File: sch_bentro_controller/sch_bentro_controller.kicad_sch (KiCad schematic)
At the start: 11 parts, among them J1 Barrel_Jack, J2 Screw_Terminal_01x02, Q1 BSS214, SW1 SW_Push, SW2 RockerSwitch

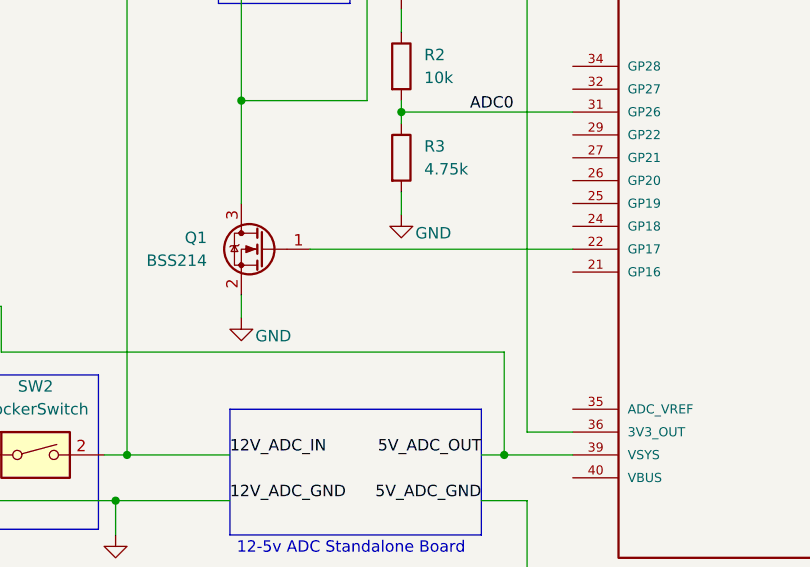
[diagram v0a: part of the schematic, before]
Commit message: added Gate pull down resistor
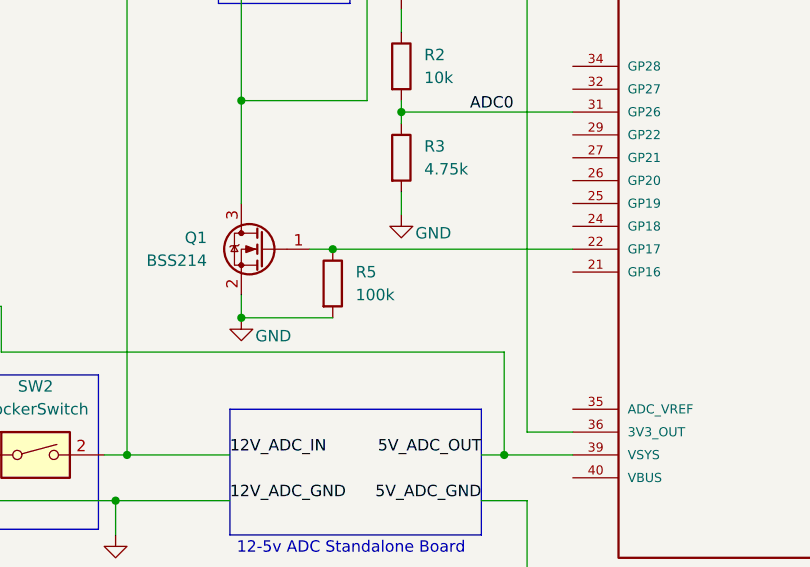
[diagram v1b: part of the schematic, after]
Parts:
- added R5: 100k, symbol Device:R
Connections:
- net GND: now also R5.2
- net at A1.22 (GP17), Q1.1 (G): now also R5.1
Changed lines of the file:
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@@
+	)
+	(junction
+		(at 106.68 111.76)
+		(diameter 0)
+		(color 0 0 0 0)
 	)
 	(junction
@@
 	)
 	(junction
+		(at 96.52 119.38)
+		(diameter 0)
+		(color 0 0 0 0)
+	)
+	(junction
 		(at 125.73 134.62)
 		(diameter 0)
@@
 	(wire
 		(pts
-			(xy 104.14 111.76) (xy 133.35 111.76)
+			(xy 104.14 111.76) (xy 106.68 111.76)
 		)
 		(stroke
@@
 	(wire
 		(pts
+			(xy 96.52 119.38) (xy 106.68 119.38)
+		)
+		(stroke
+			(width 0)
+			(type default)
+		)
+	)
+	(wire
+		(pts
 			(xy 195.58 154.94) (xy 195.58 153.67)
 		)
@@
 		(pts
 			(xy 184.15 91.44) (xy 199.39 91.44)
+		)
+		(stroke
+			(width 0)
+			(type default)
+		)
+	)
+	(wire
+		(pts
+			(xy 106.68 111.76) (xy 133.35 111.76)
 		)
 		(stroke
@@
 					(unit 1)
 				)
+			)
+		)
+	)
+	(symbol
+		(lib_id "Device:R")
+		(at 106.68 115.57 0)
+		(unit 1)
+		(exclude_from_sim no)
+		(in_bom yes)
+		(on_board yes)
+		(dnp no)
+		(fields_autoplaced yes)
+		(property "Reference" "R5"
+			(at 109.22 114.2999 0)
+			(effects
+				(font
+					(size 1.27 1.27)
+				)
+				(justify left)
+			)
+		)
+		(property "Value" "100k"
+			(at 109.22 116.8399 0)
+			(effects
+				(font
+					(size 1.27 1.27)
+				)
+				(justify left)
+			)
+		)
+		(property "Footprint" ""
+			(at 104.902 115.57 90)
+			(effects
+				(font
+					(size 1.27 1.27)
+				)
+				(hide yes)
+			)
+		)
+		(property "Datasheet" "~"
+			(at 106.68 115.57 0)
+			(effects
+				(font
+					(size 1.27 1.27)
+				)
+				(hide yes)
+			)
+		)
+		(property "Description" "Resistor"
+			(at 106.68 115.57 0)
+			(effects
+				(font
+					(size 1.27 1.27)
+				)
+				(hide yes)
+			)
+		)
+		(pin "2"
+		)
+		(pin "1"
+		)
+		(instances
+			(project "sch_bentro_controller"
+				(path "/4c494bf6-61ac-4c54-bb68-d6309caa82e3"
+					(reference "R5")
+					(unit 1)
+				)
